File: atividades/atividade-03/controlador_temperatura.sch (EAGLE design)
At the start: 28 parts, among them Q1 BC337, Q2 BC337, Q3 BC337

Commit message: oneWire buss scheme label add
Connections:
- net N$15 renamed D7
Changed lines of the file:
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@@
 </segment>
 </net>
-<net name="N$15" class="0">
+<net name="D7" class="0">
 <segment>
 <pinref part="DS18B20" gate="-2" pin="KL"/>
 <pinref part="R12" gate="G$1" pin="2"/>
 <wire x1="170.18" y1="-22.86" x2="162.56" y2="-22.86" width="0.1524" layer="91"/>
+<wire x1="162.56" y1="-22.86" x2="157.48" y2="-22.86" width="0.1524" layer="91"/>
+<junction x="162.56" y="-22.86"/>
+<label x="152.4" y="-22.86" size="1.778" layer="95"/>
 </segment>
 </net>

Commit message: buttons scheme labels add
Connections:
- net N$10 renamed A0
- net N$11 renamed A1
- net N$12 renamed A2
- net N$13 renamed A3
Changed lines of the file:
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@@
 </segment>
 </net>
-<net name="N$10" class="0">
+<net name="A0" class="0">
 <segment>
 <pinref part="BUTTONS" gate="G$1" pin="5"/>
@@
 <pinref part="R8" gate="G$1" pin="2"/>
 <wire x1="167.64" y1="35.56" x2="172.72" y2="35.56" width="0.1524" layer="91"/>
+<label x="167.64" y="35.56" size="1.778" layer="95" rot="R270"/>
 </segment>
 </net>
-<net name="N$11" class="0">
+<net name="A1" class="0">
 <segment>
 <pinref part="R9" gate="G$1" pin="2"/>
@@
 <pinref part="BUTTONS" gate="G$1" pin="4"/>
 <wire x1="165.1" y1="27.94" x2="165.1" y2="48.26" width="0.1524" layer="91"/>
+<label x="165.1" y="27.94" size="1.778" layer="95" rot="R270"/>
 </segment>
 </net>
-<net name="N$12" class="0">
+<net name="A2" class="0">
 <segment>
 <pinref part="R10" gate="G$1" pin="2"/>
@@
 <pinref part="BUTTONS" gate="G$1" pin="3"/>
 <wire x1="162.56" y1="20.32" x2="162.56" y2="48.26" width="0.1524" layer="91"/>
+<label x="162.56" y="20.32" size="1.778" layer="95" rot="R270"/>
 </segment>
 </net>
-<net name="N$13" class="0">
+<net name="A3" class="0">
 <segment>
 <pinref part="R11" gate="G$1" pin="2"/>
@@
 <pinref part="BUTTONS" gate="G$1" pin="2"/>
 <wire x1="160.02" y1="12.7" x2="160.02" y2="48.26" width="0.1524" layer="91"/>
+<label x="160.02" y="12.7" size="1.778" layer="95" rot="R270"/>
 </segment>
 </net>

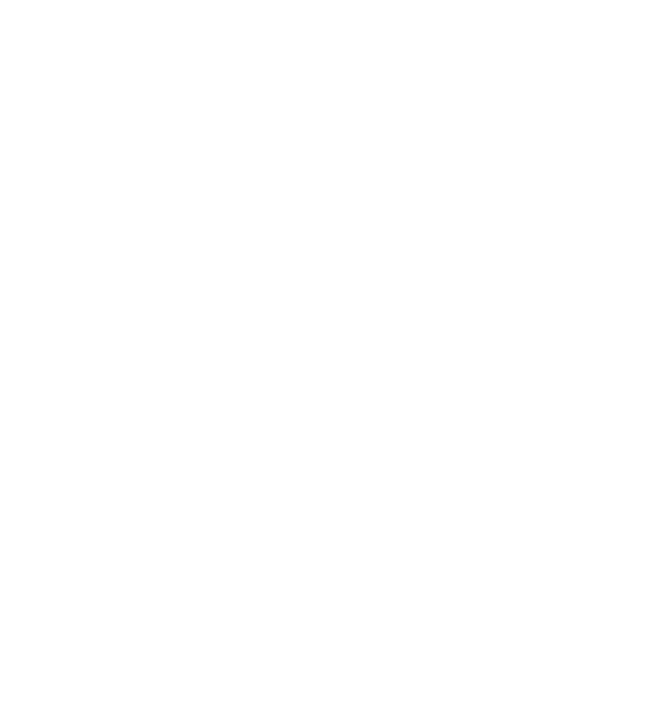
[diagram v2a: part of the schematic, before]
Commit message: conectores shield arduino scheme
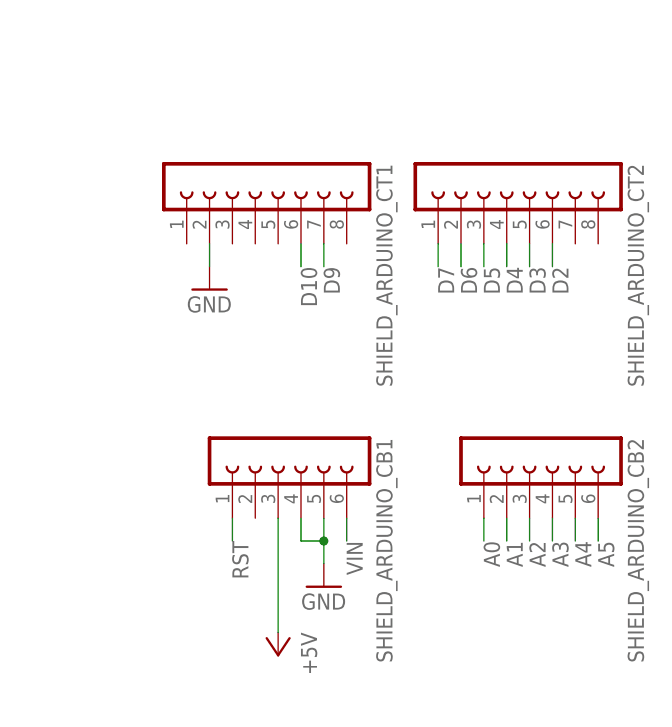
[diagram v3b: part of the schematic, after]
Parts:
- added SHIELD_ARDUINO_CB1, SHIELD_ARDUINO_CB2: (no value), con-lsta:FE06-1
- added SHIELD_ARDUINO_CT1, SHIELD_ARDUINO_CT2: (no value), con-lsta:FE08-1
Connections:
- net A0: now also SHIELD_ARDUINO_CB2.1
- net A1: now also SHIELD_ARDUINO_CB2.2
- net A2: now also SHIELD_ARDUINO_CB2.3
- net A3: now also SHIELD_ARDUINO_CB2.4
- net A4: now also SHIELD_ARDUINO_CB2.5
- net A5: now also SHIELD_ARDUINO_CB2.6
- net D10: now also SHIELD_ARDUINO_CT1.6
- net D2: now also SHIELD_ARDUINO_CT2.6
- net D3: now also SHIELD_ARDUINO_CT2.5
- net D4: now also SHIELD_ARDUINO_CT2.4
- net D5: now also SHIELD_ARDUINO_CT2.3
- net D6: now also SHIELD_ARDUINO_CT2.2
- net D7: now also SHIELD_ARDUINO_CT2.1
- net D9: now also SHIELD_ARDUINO_CT1.7
- net GND: now also SHIELD_ARDUINO_CB1.4, SHIELD_ARDUINO_CB1.5, SHIELD_ARDUINO_CT1.2
- net RST: now also SHIELD_ARDUINO_CB1.1
- net VCC: now also SHIELD_ARDUINO_CB1.3
- net VIN: now also SHIELD_ARDUINO_CB1.6
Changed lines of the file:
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@@
 <part name="R12" library="resistor-power" library_urn="urn:adsk.eagle:library:344" deviceset="R" device="RS1/8" package3d_urn="urn:adsk.eagle:package:25168/1" value="4.7k"/>
 <part name="GND10" library="supply1" library_urn="urn:adsk.eagle:library:371" deviceset="GND" device=""/>
+<part name="SHIELD_ARDUINO_CB1" library="con-lsta" library_urn="urn:adsk.eagle:library:161" deviceset="FE06-1" device="" package3d_urn="urn:adsk.eagle:package:8191/1"/>
+<part name="SHIELD_ARDUINO_CT1" library="con-lsta" library_urn="urn:adsk.eagle:library:161" deviceset="FE08-1" device="" package3d_urn="urn:adsk.eagle:package:8194/1"/>
+<part name="SHIELD_ARDUINO_CT2" library="con-lsta" library_urn="urn:adsk.eagle:library:161" deviceset="FE08-1" device="" package3d_urn="urn:adsk.eagle:package:8194/1"/>
+<part name="SHIELD_ARDUINO_CB2" library="con-lsta" library_urn="urn:adsk.eagle:library:161" deviceset="FE06-1" device="" package3d_urn="urn:adsk.eagle:package:8191/1"/>
+<part name="GND11" library="supply1" library_urn="urn:adsk.eagle:library:371" deviceset="GND" device=""/>
+<part name="GND12" library="supply1" library_urn="urn:adsk.eagle:library:371" deviceset="GND" device=""/>
+<part name="P+6" library="supply1" library_urn="urn:adsk.eagle:library:371" deviceset="VCC" device="" value="+5V"/>
 </parts>
 <sheets>
@@
 <instance part="GND10" gate="1" x="165.1" y="-27.94" smashed="yes" rot="R270">
 <attribute name="VALUE" x="162.56" y="-25.4" size="1.778" layer="96" rot="R270"/>
+</instance>
+<instance part="SHIELD_ARDUINO_CB1" gate="G$1" x="198.12" y="-83.82" smashed="yes" rot="R270">
+<attribute name="VALUE" x="187.96" y="-82.55" size="1.778" layer="96" rot="R270"/>
+<attribute name="NAME" x="209.042" y="-82.55" size="1.778" layer="95" rot="R270"/>
+</instance>
+<instance part="SHIELD_ARDUINO_CT1" gate="G$1" x="195.58" y="-53.34" smashed="yes" rot="R270">
+<attribute name="VALUE" x="182.88" y="-52.07" size="1.778" layer="96" rot="R270"/>
+<attribute name="NAME" x="209.042" y="-52.07" size="1.778" layer="95" rot="R270"/>
+</instance>
+<instance part="SHIELD_ARDUINO_CT2" gate="G$1" x="223.52" y="-53.34" smashed="yes" rot="R270">
+<attribute name="VALUE" x="210.82" y="-52.07" size="1.778" layer="96" rot="R270"/>
+<attribute name="NAME" x="236.982" y="-52.07" size="1.778" layer="95" rot="R270"/>
+</instance>
+<instance part="SHIELD_ARDUINO_CB2" gate="G$1" x="226.06" y="-83.82" smashed="yes" rot="R270">
+<attribute name="VALUE" x="215.9" y="-82.55" size="1.778" layer="96" rot="R270"/>
+<attribute name="NAME" x="236.982" y="-82.55" size="1.778" layer="95" rot="R270"/>
+</instance>
+<instance part="GND11" gate="1" x="190.5" y="-66.04" smashed="yes">
+<attribute name="VALUE" x="187.96" y="-68.58" size="1.778" layer="96"/>
+</instance>
+<instance part="GND12" gate="1" x="203.2" y="-99.06" smashed="yes">
+<attribute name="VALUE" x="200.66" y="-101.6" size="1.778" layer="96"/>
+</instance>
+<instance part="P+6" gate="VCC" x="198.12" y="-106.68" smashed="yes" rot="R180">
+<attribute name="VALUE" x="200.66" y="-104.14" size="1.778" layer="96" rot="R270"/>
 </instance>
 </instances>
@@
 <wire x1="170.18" y1="-27.94" x2="167.64" y2="-27.94" width="0.1524" layer="91"/>
 </segment>
+<segment>
+<pinref part="SHIELD_ARDUINO_CT1" gate="G$1" pin="2"/>
+<pinref part="GND11" gate="1" pin="GND"/>
+<wire x1="190.5" y1="-60.96" x2="190.5" y2="-63.5" width="0.1524" layer="91"/>
+</segment>
+<segment>
+<pinref part="SHIELD_ARDUINO_CB1" gate="G$1" pin="5"/>
+<pinref part="GND12" gate="1" pin="GND"/>
+<wire x1="203.2" y1="-91.44" x2="203.2" y2="-93.98" width="0.1524" layer="91"/>
+<pinref part="SHIELD_ARDUINO_CB1" gate="G$1" pin="4"/>
+<wire x1="203.2" y1="-93.98" x2="203.2" y2="-96.52" width="0.1524" layer="91"/>
+<wire x1="200.66" y1="-91.44" x2="200.66" y2="-93.98" width="0.1524" layer="91"/>
+<wire x1="200.66" y1="-93.98" x2="203.2" y2="-93.98" width="0.1524" layer="91"/>
+<junction x="203.2" y="-93.98"/>
+</segment>
 </net>
 <net name="N$1" class="0">
@@
 <label x="106.68" y="-12.7" size="1.778" layer="95"/>
 </segment>
+<segment>
+<pinref part="SHIELD_ARDUINO_CB1" gate="G$1" pin="6"/>
+<wire x1="205.74" y1="-91.44" x2="205.74" y2="-93.98" width="0.1524" layer="91"/>
+<label x="205.74" y="-93.98" size="1.778" layer="95" rot="R270"/>
+</segment>
 </net>
 <net name="N$5" class="0">
@@
 <wire x1="-20.32" y1="50.8" x2="-25.4" y2="50.8" width="0.1524" layer="91"/>
 <label x="-30.48" y="50.8" size="1.778" layer="95"/>
+</segment>
+<segment>
+<pinref part="SHIELD_ARDUINO_CT1" gate="G$1" pin="7"/>
+<wire x1="203.2" y1="-60.96" x2="203.2" y2="-63.5" width="0.1524" layer="91"/>
+<label x="203.2" y="-63.5" size="1.778" layer="95" rot="R270"/>
 </segment>
 </net>
@@
 <label x="-33.02" y="2.54" size="1.778" layer="95"/>
 </segment>
+<segment>
+<pinref part="SHIELD_ARDUINO_CT2" gate="G$1" pin="2"/>
+<wire x1="218.44" y1="-60.96" x2="218.44" y2="-63.5" width="0.1524" layer="91"/>
+<label x="218.44" y="-63.5" size="1.778" layer="95" rot="R270"/>
+</segment>
 </net>
 <net name="N$7" class="0">
@@
 <wire x1="86.36" y1="35.56" x2="86.36" y2="30.48" width="0.1524" layer="91"/>
 <label x="86.36" y="30.48" size="1.778" layer="95" rot="R270"/>
+</segment>
+<segment>
+<pinref part="SHIELD_ARDUINO_CB2" gate="G$1" pin="5"/>
+<wire x1="231.14" y1="-91.44" x2="231.14" y2="-93.98" width="0.1524" layer="91"/>
+<label x="231.14" y="-93.98" size="1.778" layer="95" rot="R270"/>
 </segment>
 </net>
@@
 <junction x="167.64" y="-12.7"/>
 </segment>
+<segment>
+<pinref part="SHIELD_ARDUINO_CB1" gate="G$1" pin="3"/>
+<pinref part="P+6" gate="VCC" pin="VCC"/>
+<wire x1="198.12" y1="-91.44" x2="198.12" y2="-104.14" width="0.1524" layer="91"/>
+</segment>
 </net>
 <net name="A5" class="0">
@@
 <label x="91.44" y="30.48" size="1.778" layer="95" rot="R270"/>
 </segment>
+<segment>
+<pinref part="SHIELD_ARDUINO_CB2" gate="G$1" pin="6"/>
+<wire x1="233.68" y1="-91.44" x2="233.68" y2="-93.98" width="0.1524" layer="91"/>
+<label x="233.68" y="-93.98" size="1.778" layer="95" rot="R270"/>
+</segment>
 </net>
 <net name="D2" class="0">
@@
 <label x="104.14" y="30.48" size="1.778" layer="95" rot="R270"/>
 </segment>
+<segment>
+<pinref part="SHIELD_ARDUINO_CT2" gate="G$1" pin="6"/>
+<wire x1="228.6" y1="-60.96" x2="228.6" y2="-63.5" width="0.1524" layer="91"/>
+<label x="228.6" y="-63.5" size="1.778" layer="95" rot="R270"/>
+</segment>
 </net>
 <net name="D3" class="0">
@@
 <label x="106.68" y="30.48" size="1.778" layer="95" rot="R270"/>
 </segment>
+<segment>
+<pinref part="SHIELD_ARDUINO_CT2" gate="G$1" pin="5"/>
+<wire x1="226.06" y1="-60.96" x2="226.06" y2="-63.5" width="0.1524" layer="91"/>
+<label x="226.06" y="-63.5" size="1.778" layer="95" rot="R270"/>
+</segment>
 </net>
 <net name="D4" class="0">
@@
 <label x="109.22" y="30.48" size="1.778" layer="95" rot="R270"/>
 </segment>
+<segment>
+<pinref part="SHIELD_ARDUINO_CT2" gate="G$1" pin="4"/>
+<wire x1="223.52" y1="-60.96" x2="223.52" y2="-63.5" width="0.1524" layer="91"/>
+<label x="223.52" y="-63.5" size="1.778" layer="95" rot="R270"/>
+</segment>
 </net>
 <net name="D5" class="0">
@@
 <wire x1="111.76" y1="35.56" x2="111.76" y2="30.48" width="0.1524" layer="91"/>
 <label x="111.76" y="30.48" size="1.778" layer="95" rot="R270"/>
+</segment>
+<segment>
+<pinref part="SHIELD_ARDUINO_CT2" gate="G$1" pin="3"/>
+<wire x1="220.98" y1="-60.96" x2="220.98" y2="-63.5" width="0.1524" layer="91"/>
+<label x="220.98" y="-63.5" size="1.778" layer="95" rot="R270"/>
 </segment>
 </net>
@@
 <label x="78.74" y="-7.62" size="1.778" layer="95"/>
 </segment>
+<segment>
+<pinref part="SHIELD_ARDUINO_CT1" gate="G$1" pin="6"/>
+<wire x1="200.66" y1="-60.96" x2="200.66" y2="-63.5" width="0.1524" layer="91"/>
+<label x="200.66" y="-63.5" size="1.778" layer="95" rot="R270"/>
+</segment>
 </net>
 <net name="RST" class="0">
@@
 <wire x1="101.6" y1="-45.72" x2="99.06" y2="-45.72" width="0.1524" layer="91"/>
 <label x="93.98" y="-45.72" size="1.778" layer="95"/>
+</segment>
+<segment>
+<pinref part="SHIELD_ARDUINO_CB1" gate="G$1" pin="1"/>
+<wire x1="193.04" y1="-91.44" x2="193.04" y2="-93.98" width="0.1524" layer="91"/>
+<label x="193.04" y="-93.98" size="1.778" layer="95" rot="R270"/>
 </segment>
 </net>
@@
 <label x="167.64" y="35.56" size="1.778" layer="95" rot="R270"/>
 </segment>
+<segment>
+<pinref part="SHIELD_ARDUINO_CB2" gate="G$1" pin="1"/>
+<wire x1="220.98" y1="-91.44" x2="220.98" y2="-93.98" width="0.1524" layer="91"/>
+<label x="220.98" y="-93.98" size="1.778" layer="95" rot="R270"/>
+</segment>
 </net>
 <net name="A1" class="0">
@@
 <label x="165.1" y="27.94" size="1.778" layer="95" rot="R270"/>
 </segment>
+<segment>
+<pinref part="SHIELD_ARDUINO_CB2" gate="G$1" pin="2"/>
+<wire x1="223.52" y1="-91.44" x2="223.52" y2="-93.98" width="0.1524" layer="91"/>
+<label x="223.52" y="-93.98" size="1.778" layer="95" rot="R270"/>
+</segment>
 </net>
 <net name="A2" class="0">
@@
 <label x="162.56" y="20.32" size="1.778" layer="95" rot="R270"/>
 </segment>
+<segment>
+<pinref part="SHIELD_ARDUINO_CB2" gate="G$1" pin="3"/>
+<wire x1="226.06" y1="-91.44" x2="226.06" y2="-93.98" width="0.1524" layer="91"/>
+<label x="226.06" y="-93.98" size="1.778" layer="95" rot="R270"/>
+</segment>
 </net>
 <net name="A3" class="0">
@@
 <wire x1="160.02" y1="12.7" x2="160.02" y2="48.26" width="0.1524" layer="91"/>
 <label x="160.02" y="12.7" size="1.778" layer="95" rot="R270"/>
+</segment>
+<segment>
+<pinref part="SHIELD_ARDUINO_CB2" gate="G$1" pin="4"/>
+<wire x1="228.6" y1="-91.44" x2="228.6" y2="-93.98" width="0.1524" layer="91"/>
+<label x="228.6" y="-93.98" size="1.778" layer="95" rot="R270"/>
 </segment>
 </net>
@@
 <label x="152.4" y="-22.86" size="1.778" layer="95"/>
 </segment>
-</net>
+<segment>
+<pinref part="SHIELD_ARDUINO_CT2" gate="G$1" pin="1"/>
+<wire x1="215.9" y1="-60.96" x2="215.9" y2="-63.5" width="0.1524" layer="91"/>
+<label x="215.9" y="-63.5" size="1.778" layer="95" rot="R270"/>
+</segment>
+</net>
